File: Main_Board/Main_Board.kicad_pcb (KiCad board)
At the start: 4 copper layers, 45 x 38.4 mm, 128 parts, among them IC1 TPS25200DRVR, J1 RESET, J2 MAIN_UART, J3 Baterry input, J4 External bords interfaces, J7 Terminal, J8 Terminal, Q1 2N7002, Q10 FDN339AN, Q7 MMBT3904LT1G, Q8 FDN339AN, Q9 MMBT3904LT1G, U1 W25Q128JVS, U2 ESP32-S3-MINI-1U, U3 TPS63031DSK, U4 TPS63031DSK, U5 TLV61070ADBV, U6 SS351AT, U7 THVD1450DR

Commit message: ADC Vin ready
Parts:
- C7, R15, R16, R17: moved to B.Cu
- moved C7 57.0 mm to (93.1, 85.8), turned to 90 degrees
- moved R16 56.2 mm to (94.1, 90.7), turned to 180 degrees
- moved R15 55.8 mm to (98.5, 92.1), turned to 180 degrees
- moved R17 53.6 mm to (94.0, 89.2), turned to 180 degrees
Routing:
- net /ESP32/Vin_ADC: track 0.00 -> 5.10 mm, vias 0 -> 1
- net Net-(R15-Pad2): track 0.00 -> 4.87 mm
- net /PSU/Back_Boost1/V_In: track 49.2 -> 53.1 mm
- net +3V3_MB: track 21.6 -> 19.7 mm, vias 12 -> 11
- net Net-(U2-IO4): track 3.87 -> 4.59 mm

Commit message: 5V Ready
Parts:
- moved R21 36.4 mm to (99.9, 110.5), turned to -90 degrees
- moved R25 31.6 mm to (109.1, 96.1), turned to -90 degrees
- moved R24 28.8 mm to (110.6, 96.1), turned to 90 degrees
- moved R39 1.45 mm to (102.6, 110.9)
- moved D12 0.40 mm to (103.1, 105.9)
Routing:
- net +5V: track 3.30 -> 32.2 mm, vias 0 -> 2
- net /ESP32/5V_PG: track 0.00 -> 15.5 mm, vias 0 -> 2
- net /PSU/Boost/V_out: track 22.4 -> 26.9 mm
- net Net-(U2-TXD0): track 11.7 -> 14.1 mm
- net Net-(J4-Pin_1): track 32.0 -> 33.7 mm
- net Net-(U2-RXD0): track 13.8 -> 14.8 mm
- net /Interfaces/B_RS485: track 20.3 -> 21.0 mm
- net /Interfaces/A_RS485: track 15.6 -> 16.2 mm

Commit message: Mag Arm ready
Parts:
- moved R23 41.1 mm to (80.0, 94.1), turned to -90 degrees
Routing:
- net /PSU/Input_Protection/Vbatt: track 1.69 -> 39.9 mm, vias 0 -> 1
- net Net-(IC1-EN): track 9.79 -> 45.4 mm, vias 0 -> 1
- net +3V3: track 8.98 -> 34.8 mm, vias 2 -> 3
- net /PSU/Back_Boost2/V_out: track 9.60 -> 12.4 mm
- net VBUS: track 70.8 -> 72.4 mm
- net /ESP32/5V_PG: track 15.5 -> 16.4 mm

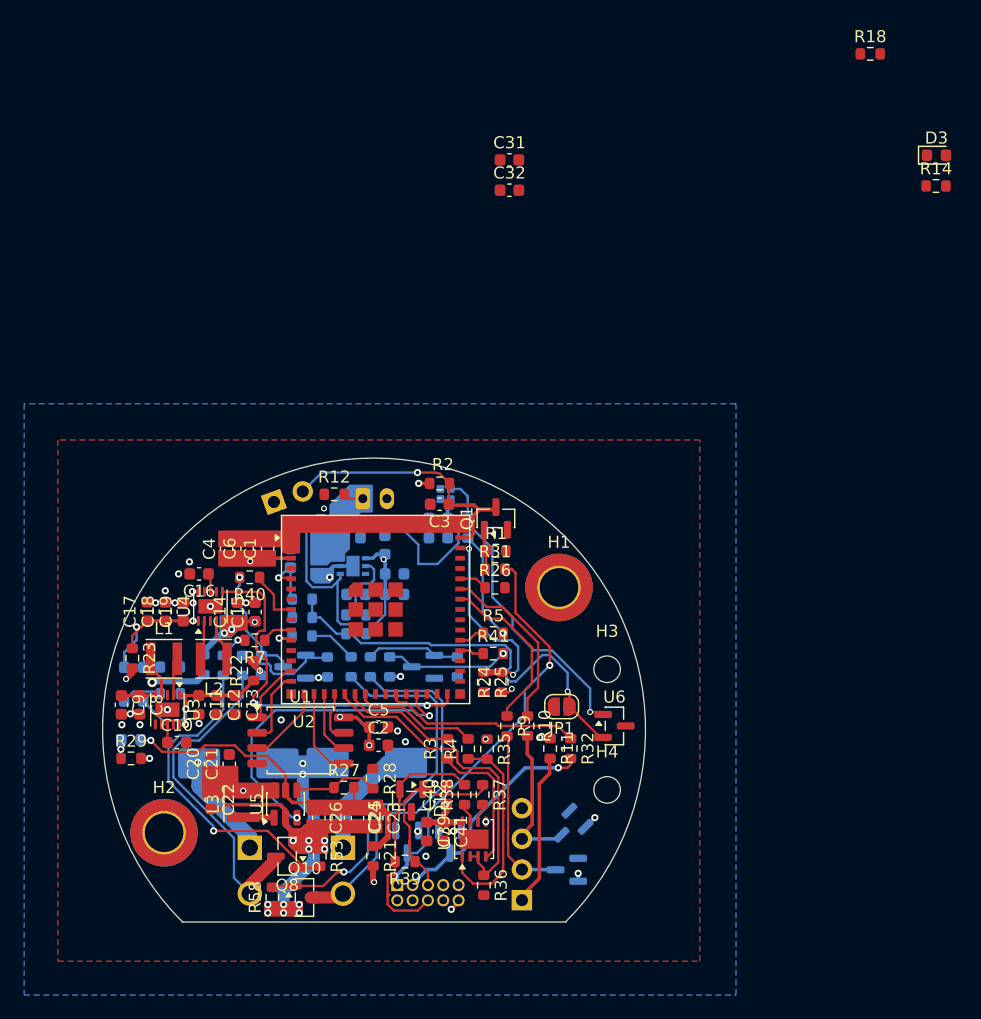
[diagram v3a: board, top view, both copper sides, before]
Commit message: LED, EN, Delete legacy
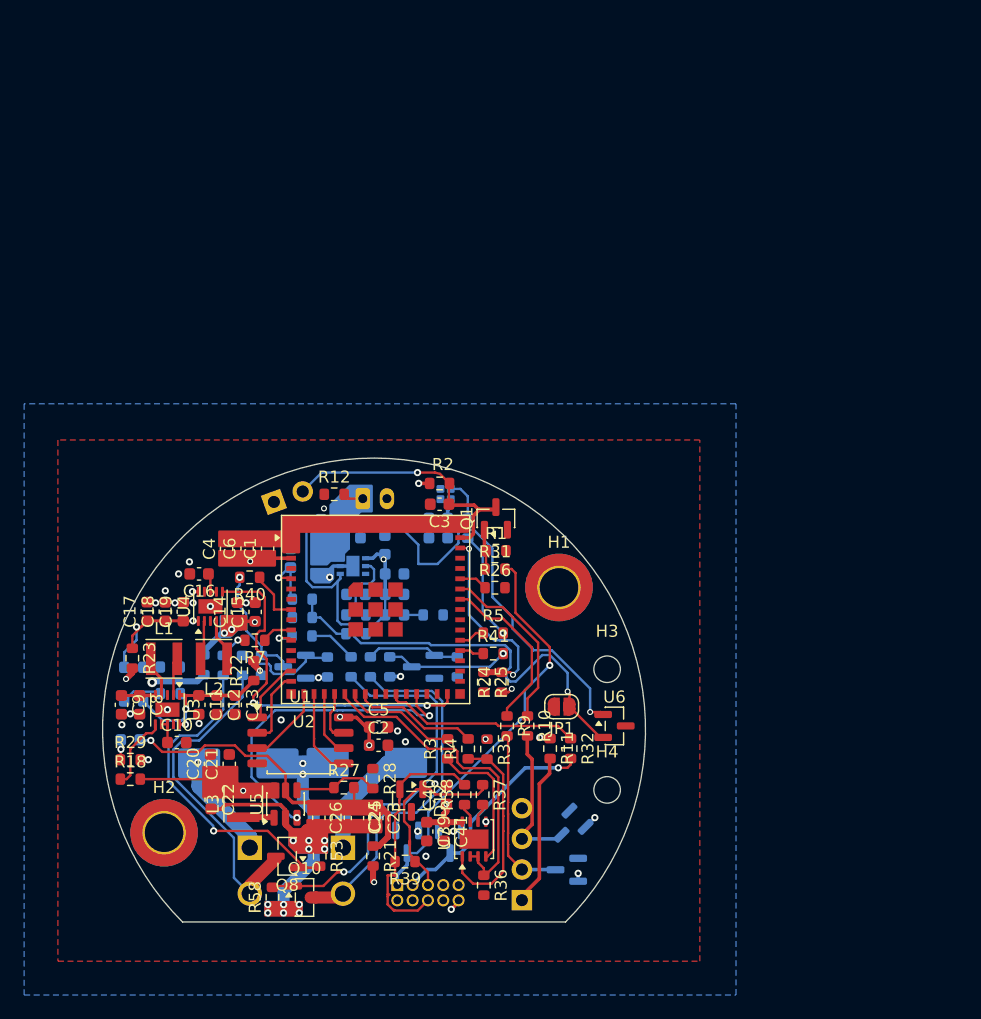
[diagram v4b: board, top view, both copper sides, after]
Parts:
- removed C31: 10uF, Capacitor_SMD:C_0603_1608Metric
- removed C32: 100nF, Capacitor_SMD:C_0603_1608Metric
- D3, R14: moved to B.Cu
- moved R18 85.9 mm to (79.8, 104.1)
- moved D3 58.9 mm to (101.7, 90.5), turned to 180 degrees
- moved R14 54.8 mm to (104.9, 90.5)
- moved R29 0.12 mm to (79.8, 102.5)
- moved D6 0.06 mm to (79.8, 100.9)
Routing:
- net /PSU/Back_Boost1/V_In: track 53.1 -> 59.9 mm
- net /PSU/Back_Boost1/EN: track 0.00 -> 6.33 mm
- net Net-(D3-K): track 0.00 -> 1.59 mm

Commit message: Routing cleanup
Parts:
- moved R35 0.14 mm to (109.5, 101.6)
- moved R31 0.08 mm to (110.1, 86.7)
- moved R26 0.07 mm to (110.1, 88.2)
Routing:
- net /PSU/Input_Protection/Vbatt: track 39.9 -> 37.6 mm
- net /Interfaces/A_RS485: track 16.2 -> 15.5 mm
- net /PSU/Back_Boost2/V_out: track 12.4 -> 11.8 mm
- net +3V3: vias 3 -> 4

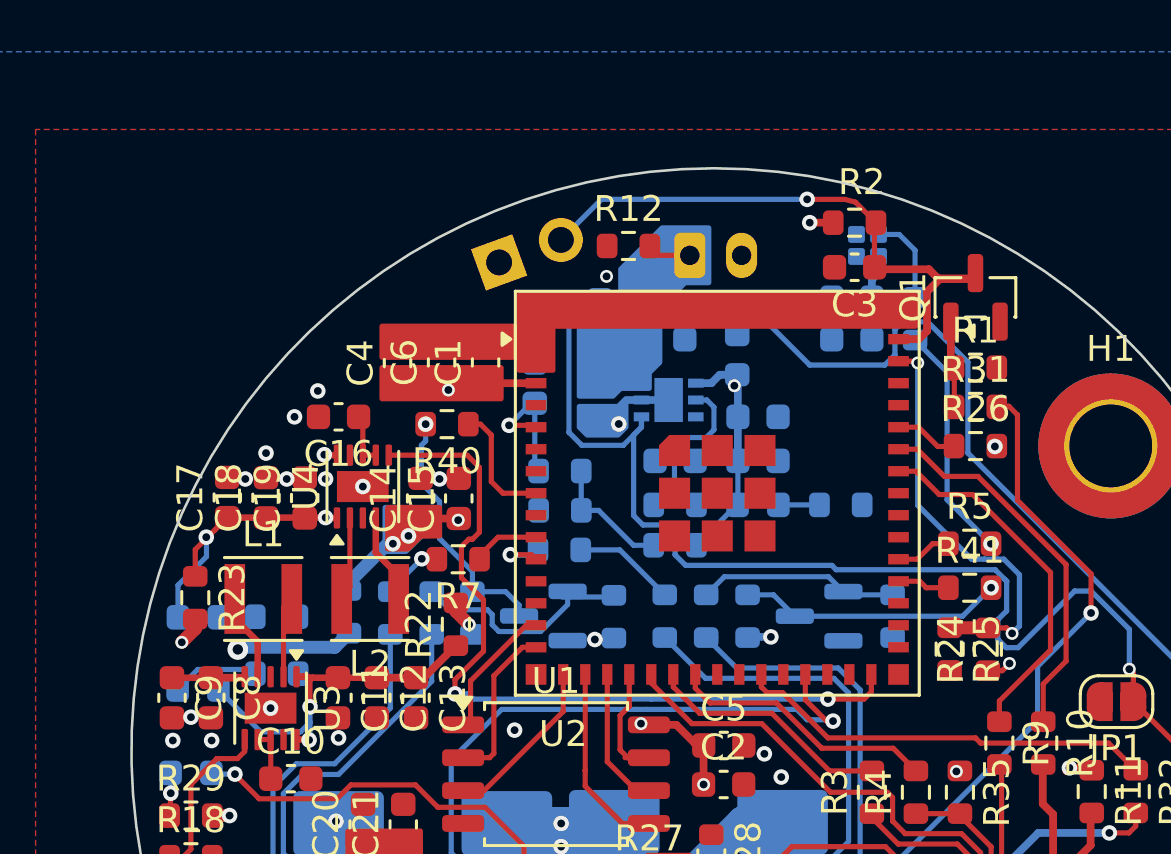
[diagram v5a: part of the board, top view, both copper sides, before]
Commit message: Routing, repin pyro continuity to IO38
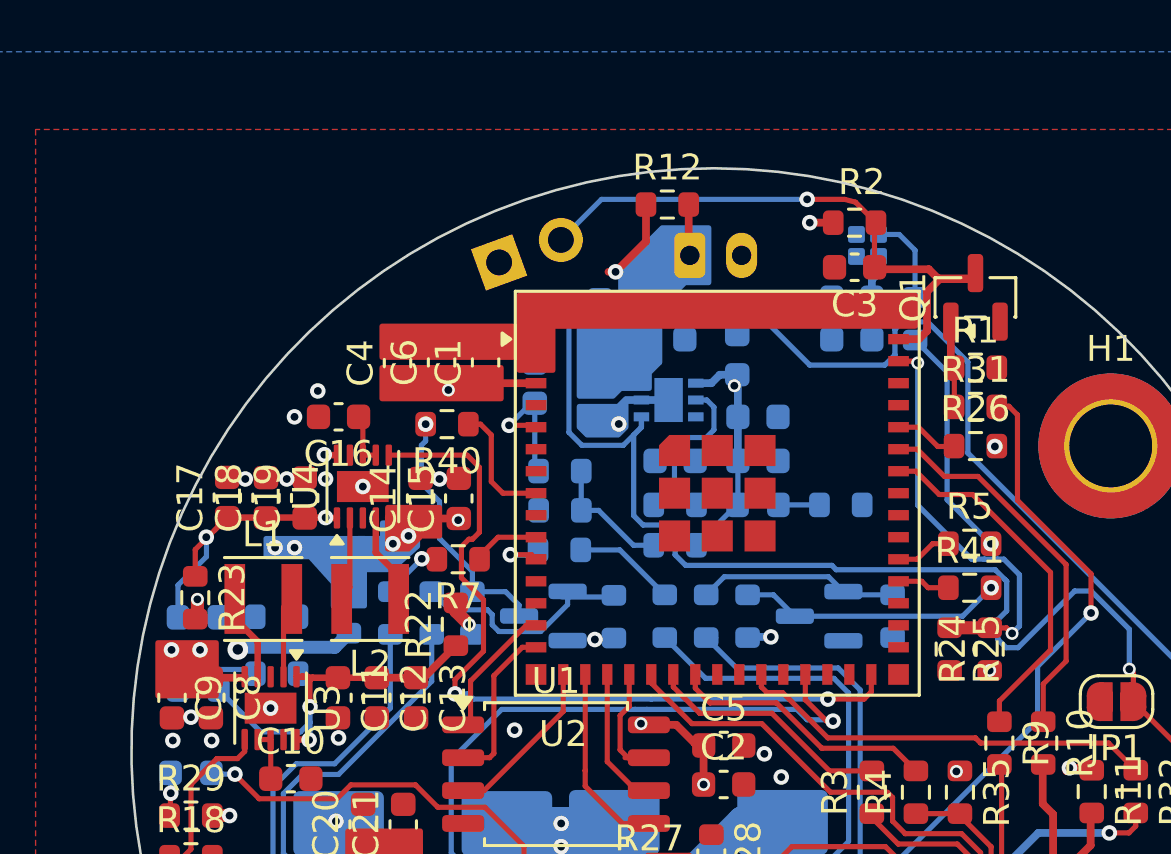
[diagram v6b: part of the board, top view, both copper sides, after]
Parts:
- moved R12 2.19 mm to (98.2, 78.9)
- moved R24 0.07 mm to (110.7, 96.1)
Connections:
- R41 pad 1: Net-(U2-IO5) -> Net-(U2-IO38)
- U2 pad 34: unconnected-(U2-IO38-Pad34) -> Net-(U2-IO38)
- U2 pad 9: Net-(U2-IO5) -> unconnected-(U2-IO5-Pad9)
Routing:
- net +3V3: track 34.8 -> 52.1 mm
- net VBUS: track 72.4 -> 75.7 mm
- net Net-(U2-IO38): track 0.00 -> 2.03 mm
- net (no net): track 2.03 -> 0.00 mm
- net +5V: track 32.1 -> 30.7 mm
- net /PSU/Back_Boost1/V_In: track 59.9 -> 60.8 mm, vias 5 -> 9
- net GND: vias 36 -> 35

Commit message: Routing
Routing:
- net +3V3: track 52.1 -> 73.8 mm
- net +5V: track 30.7 -> 45.0 mm, vias 2 -> 4
- net GND: vias 35 -> 37

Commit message: Routing done
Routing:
- net GND: track 46.6 -> 50.8 mm, vias 37 -> 40
- net /PSU/Back_Boost2/V_out: track 11.8 -> 14.1 mm
- net +3V3: track 73.8 -> 73.0 mm
- net /PSU/Boost/V_out: track 26.9 -> 27.6 mm
